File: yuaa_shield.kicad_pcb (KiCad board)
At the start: 2 copper layers, 220 x 118 mm, 94 parts, among them J1 PIs, J17 adafruit temp, J18 adafruit load cell, J19 adafruit load cell, J2 N2O Encoder, J20 adafruit load cell, J21 adafruit load cell, J22 adafruit load cell, J23 adafruit load cell, J25 adafruit load cell, J26 Ethane Encoder, J27 Motor Inputs, J28 Motor Pwr, J29 Radio, J3 Battery, J4 adafruit temp, J5 adafruit temp, J6 adafruit temp, J7 Main Relays, J8 Aux Relays, K10 G5LE-1 DC5, K11 G5LE-1 DC5, K12 G5LE-1 DC5, K2 G5LE-1 DC5, K3 G5LE-1 DC5, K4 G5LE-1 DC5, K5 G5LE-1 DC5, K6 G5LE-1 DC5, K7 G5LE-1 DC5, K8 G5LE-1 DC5, K9 G5LE-1 DC5, Q1 AO3400A, Q10 AO3400A, Q11 AO3400A, Q2 AO3400A, Q3 AO3400A, Q4 AO3400A, Q5 AO3400A, Q6 AO3400A, Q7 AO3400A, Q8 AO3400A, Q9 AO3400A

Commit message: drc1
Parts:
- moved R28 0.75 mm to (61.8, 143.0)
- moved R29 0.75 mm to (69.5, 143.0)
- moved R30 0.75 mm to (95.5, 143.0)
- moved R31 0.75 mm to (88.2, 143.0)
- moved R32 0.75 mm to (123.8, 143.2)
- moved R33 0.75 mm to (115.0, 143.2)
- moved R34 0.75 mm to (153.8, 143.0)
- moved R35 0.75 mm to (146.8, 143.0)
- moved D7 0.50 mm to (92.0, 106.5)
- moved R13 0.50 mm to (86.2, 108.2)
- moved R14 0.50 mm to (92.3, 111.0)
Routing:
- net /IN1: track 192.6 -> 199.5 mm
- net /IN2: track 200.4 -> 205.8 mm
- net /Ethane Tank Heater 2 Relay: track 226.0 -> 221.7 mm
- net /IN3: track 207.8 -> 211.9 mm
- net /IN4: track 215.4 -> 219.3 mm
- net /Nitrous Tank Heater 1 Relay: track 208.1 -> 204.7 mm
- net /N2O Vent Relay: track 78.2 -> 75.9 mm
- net Net-(D5-A): track 31.8 -> 33.8 mm
- net /Ignition: track 104.5 -> 106.3 mm
- net unconnected-(A1-5V-Pad5V4): track 1.65 -> 0.00 mm
- net Net-(D1-A): track 32.9 -> 34.4 mm
- net /Ethane Encoder 1: track 119.2 -> 118.1 mm
- net Net-(J4-Pin_9): track 14.8 -> 13.8 mm
- net Net-(D6-A): track 37.5 -> 36.5 mm
- net Net-(D2-A): track 34.0 -> 34.9 mm
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
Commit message: thick traces+silkscreen
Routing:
- net +12V: track 406.2 -> 409.8 mm
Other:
- board text added: "*"
- board text added: "09/09/2026"
- board text added: "A08R"
- board text added: "A09R"
- board text added: "A10R"
- board text added: "A11R"
- board text added: "A12R"
- board text added: "A13"
- board text added: "KD"
- board text added: "MOMO"
- board text added: "PI-V:"
- board text added: "YUAA PLIQ Shield"
- board text removed: "PI-V"

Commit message: gnd plane and logo
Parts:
- added G***: LOGO, imports:yuaa_logo, F.Cu at (138.7, 68.2)
- added G***: LOGO, imports:yuaa_logo, B.Cu at (150.1, 96.2)
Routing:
- net +5VP: track 424.2 -> 316.4 mm, vias 1 -> 3
- net /SDA: track 250.9 -> 248.9 mm, vias 1 -> 3
- net /25: track 174.7 -> 175.1 mm, vias 2 -> 4
- net /SCL: track 254.9 -> 255.0 mm, vias 1 -> 3
- net /24: vias 2 -> 4
- net /Ignition: vias 2 -> 4
- net /23: vias 3 -> 5
- net /22: vias 3 -> 5

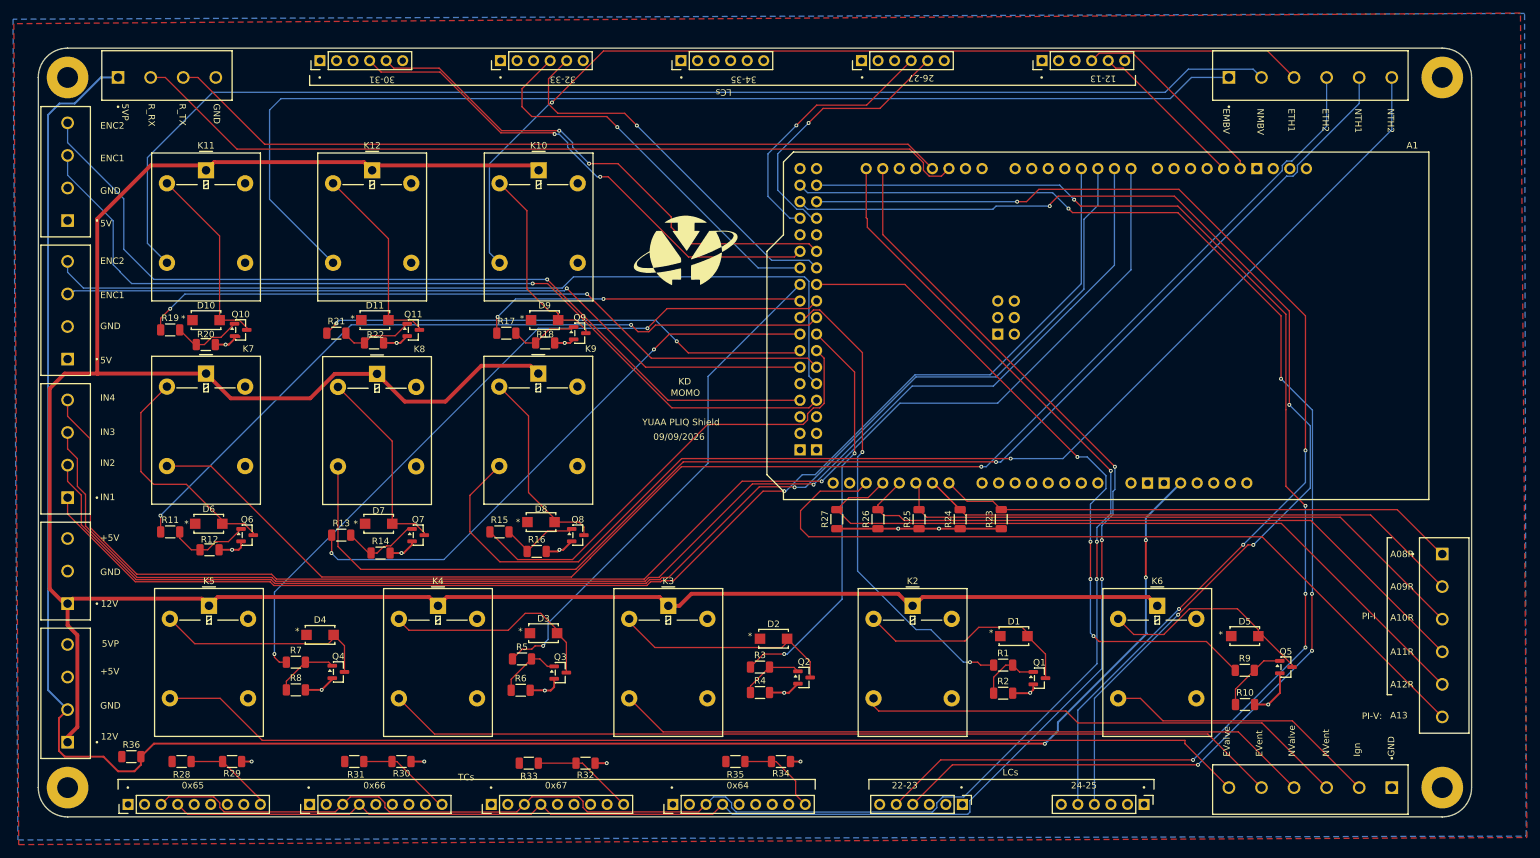
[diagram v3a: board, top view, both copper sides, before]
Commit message: flipped tc headers
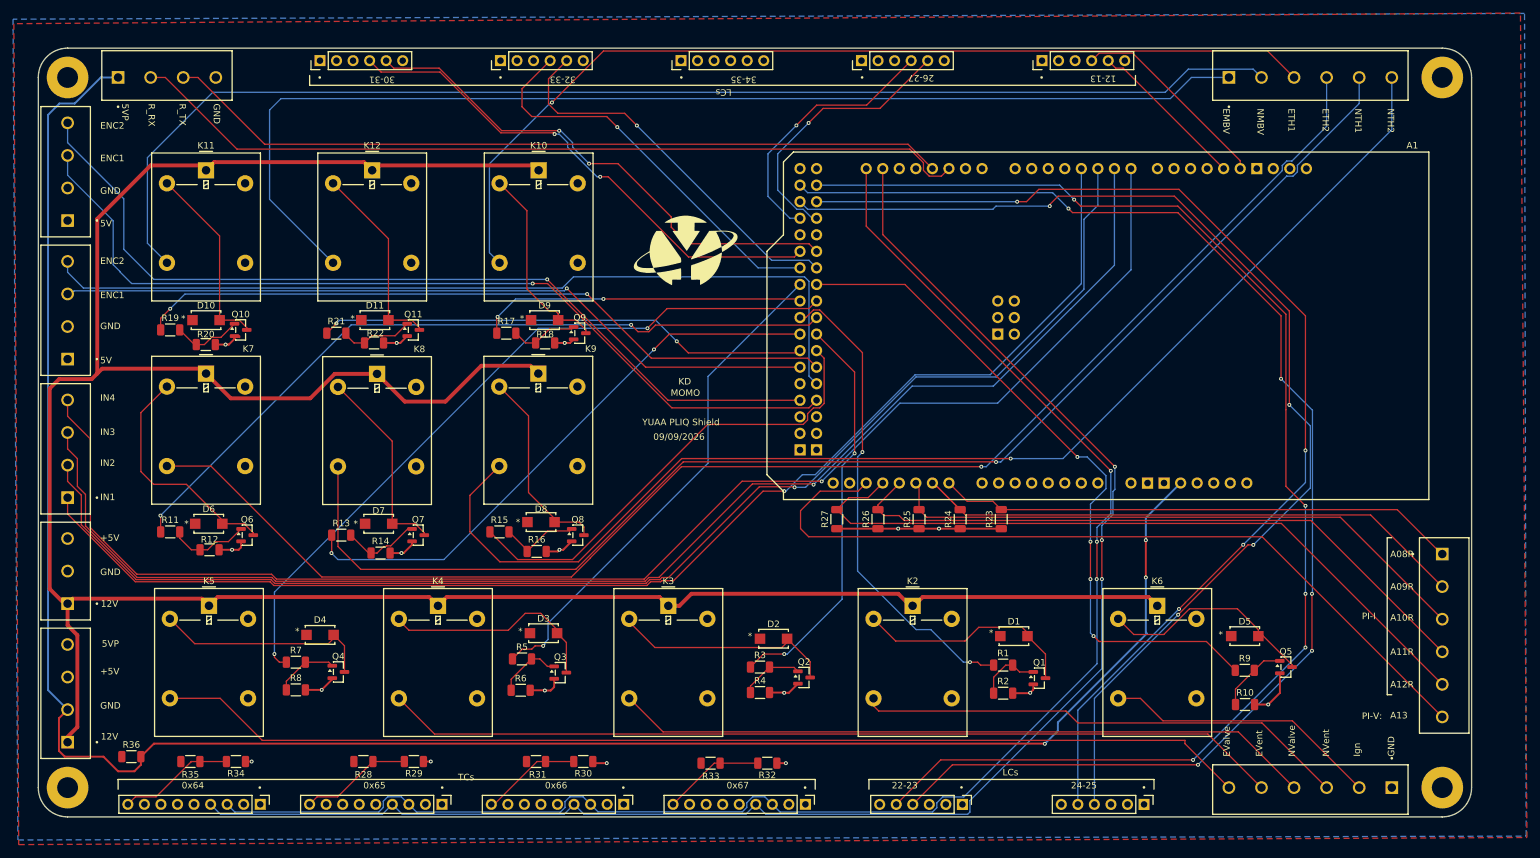
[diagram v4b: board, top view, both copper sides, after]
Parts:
- moved R34 83.7 mm to (70.1, 143.0)
- moved R35 83.7 mm to (63.1, 143.0)
- moved J6 63.3 mm to (73.8, 149.6), turned to -90 degrees
- moved J17 48.2 mm to (157.5, 149.6), turned to -90 degrees
- moved J5 48.2 mm to (129.6, 149.6), turned to -90 degrees
- moved J4 48.2 mm to (101.7, 149.6), turned to -90 degrees
- moved R28 27.9 mm to (89.7, 143.0)
- moved R29 27.9 mm to (97.4, 143.0)
- moved R30 27.9 mm to (123.4, 143.0)
- moved R31 27.9 mm to (116.2, 143.0)
- moved R32 27.9 mm to (151.7, 143.2)
- moved R33 27.9 mm to (142.9, 143.2)
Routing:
- net /SCL: track 255.0 -> 243.6 mm
- net /SDA: track 248.9 -> 243.9 mm
- net Net-(J6-Pin_9): track 13.2 -> 17.3 mm
- net Net-(J4-Pin_9): track 13.8 -> 17.3 mm
- net GND: track 83.6 -> 82.0 mm
- net +5V: track 0.00 -> 1.13 mm
- net Net-(J5-Pin_9): track 14.7 -> 15.4 mm
- net +12V: track 409.8 -> 410.4 mm
